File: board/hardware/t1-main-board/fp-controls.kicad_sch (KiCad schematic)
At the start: 6 parts

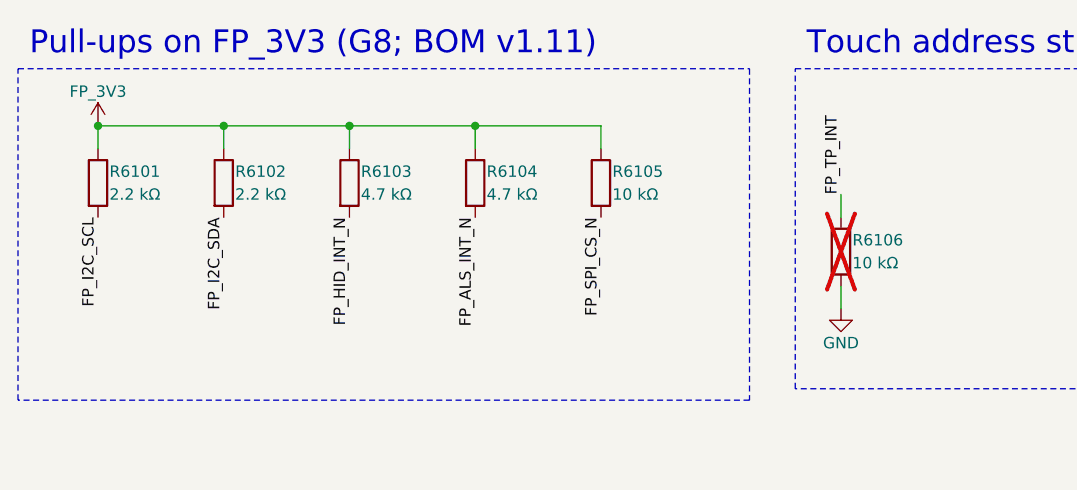
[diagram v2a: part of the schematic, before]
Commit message: NFC reader withdrawn from the board, every model (BRD-057)
Maintainer decision 2026-10-27, reason: board area. blk.nfc-reader (#42)
withdrawn: PN7160, front end, crystal, antenna contacts, NFC_VBAT switch
and link #18 removed (35 parts). BRD-057 reworded: NFC as the dynamic tag
only; blk.nfc-tag stays. Pinout v1: 1N20, A37, B38 become unconnected
spares, expander P05 a spare. BOM v1.18 item 7 (line 50: 5 switches,
lines 127-128 withdrawn), power tree v0.10, variant files, feature blocks.

Sheets after the removed one move up a page; references renumbered in
plan.py, parts.py and the specs (J6201 -> J6101 and others).

Placement v1.4: 990 parts placed, board need 96.9 % (99.1 % before),
factor 1.72; 243 capacitors within bound; DRC 0 errors; ERC 0 errors;
craft Q1 met; overlaps 0; pcb tests pass; STEP exported.

Co-Authored-By: Claude Opus 5.5 <noreply@anthropic.com>
Claude-Session: https://claude.ai/code/session_01Ei262h3TpgY9vyfNLMi5Mn
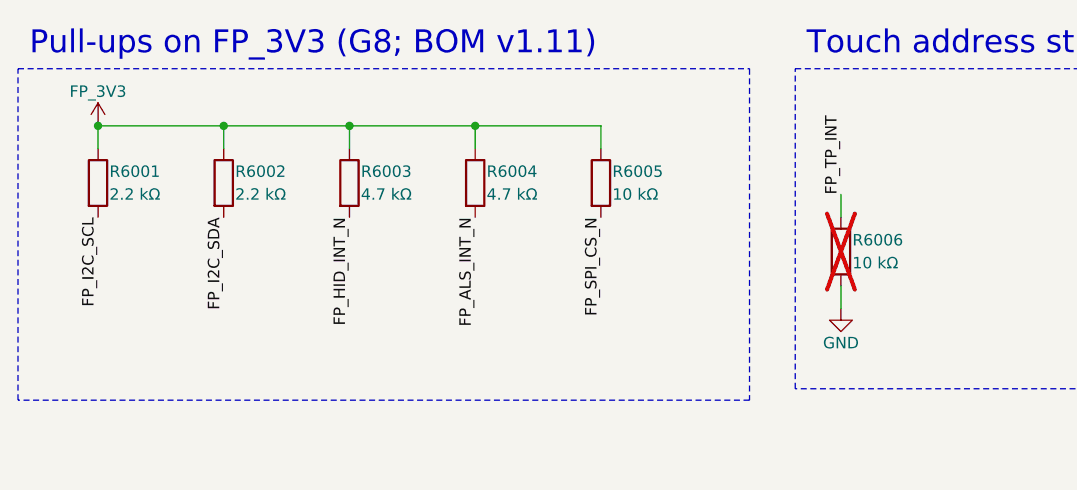
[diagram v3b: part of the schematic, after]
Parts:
- removed R6101, R6102: 2.2 kΩ, Resistor_SMD:R_0201_0603Metric, symbol Device:R
- removed R6103, R6104: 4.7 kΩ, Resistor_SMD:R_0201_0603Metric, symbol Device:R
- removed R6105, R6106: 10 kΩ, Resistor_SMD:R_0201_0603Metric, symbol Device:R
- added R6001, R6002: 2.2 kΩ, Resistor_SMD:R_0201_0603Metric, symbol Device:R
- added R6003, R6004: 4.7 kΩ, Resistor_SMD:R_0201_0603Metric, symbol Device:R
- added R6005, R6006: 10 kΩ, Resistor_SMD:R_0201_0603Metric, symbol Device:R
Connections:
- net FP_3V3: now also R6001.1, R6002.1, R6003.1, R6004.1, R6005.1
- net FP_ALS_INT_N: now also R6004.2
- net FP_HID_INT_N: now also R6003.2
- net FP_I2C_SCL: now also R6001.2
- net FP_I2C_SDA: now also R6002.2
- net FP_SPI_CS_N: now also R6005.2
- net FP_TP_INT: now also R6006.1
- net GND: now also R6006.2
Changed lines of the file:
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@@
 (title_block (title "Faceplate controls") (date "2026-10-25") (rev "A") (company "The OpenDAP Project") (comment 1 "blk.fp-controls") (comment 2 "I2C3, SPI/DBI and interrupt pulls on FP_3V3, the touch address strap"))
 (symbol (lib_id "Device:R") (at 31.75 48.26 0) (unit 1) (body_style 1) (exclude_from_sim no) (in_bom yes) (on_board yes) (dnp no)
-  (property "Reference" "R6101" (at 33.02 46.99 0) (effects (font (size 1.27 1.27)) (justify left)))
+  (property "Reference" "R6001" (at 33.02 46.99 0) (effects (font (size 1.27 1.27)) (justify left)))
   (property "Value" "2.2 kΩ" (at 33.02 49.53 0) (effects (font (size 1.27 1.27)) (justify left)))
   (property "Footprint" "Resistor_SMD:R_0201_0603Metric" (at 31.75 48.26 0) (effects (font (size 1.27 1.27))) (hide yes))
@@
   (pin "1")
   (pin "2")
-  (instances (project "t1-main-board" (path "/7746052e-d7f9-59ad-ba73-bd2b74439529/d44150e6-4ff4-595e-8942-92097db7bcde" (reference "R6101") (unit 1))))
+  (instances (project "t1-main-board" (path "/7746052e-d7f9-59ad-ba73-bd2b74439529/d44150e6-4ff4-595e-8942-92097db7bcde" (reference "R6001") (unit 1))))
 )
 (wire (pts (xy 31.75 44.45) (xy 31.75 41.91)) (stroke (width 0) (type default)))
 (symbol (lib_id "Device:R") (at 45.72 48.26 0) (unit 1) (body_style 1) (exclude_from_sim no) (in_bom yes) (on_board yes) (dnp no)
-  (property "Reference" "R6102" (at 46.99 46.99 0) (effects (font (size 1.27 1.27)) (justify left)))
+  (property "Reference" "R6002" (at 46.99 46.99 0) (effects (font (size 1.27 1.27)) (justify left)))
   (property "Value" "2.2 kΩ" (at 46.99 49.53 0) (effects (font (size 1.27 1.27)) (justify left)))
   (property "Footprint" "Resistor_SMD:R_0201_0603Metric" (at 45.72 48.26 0) (effects (font (size 1.27 1.27))) (hide yes))
@@
   (pin "1")
   (pin "2")
-  (instances (project "t1-main-board" (path "/7746052e-d7f9-59ad-ba73-bd2b74439529/d44150e6-4ff4-595e-8942-92097db7bcde" (reference "R6102") (unit 1))))
+  (instances (project "t1-main-board" (path "/7746052e-d7f9-59ad-ba73-bd2b74439529/d44150e6-4ff4-595e-8942-92097db7bcde" (reference "R6002") (unit 1))))
 )
 (wire (pts (xy 45.72 44.45) (xy 45.72 41.91)) (stroke (width 0) (type default)))
@@
 (junction (at 31.75 41.91) (diameter 0) (color 0 0 0 0))
 (symbol (lib_id "Device:R") (at 59.69 48.26 0) (unit 1) (body_style 1) (exclude_from_sim no) (in_bom yes) (on_board yes) (dnp no)
-  (property "Reference" "R6103" (at 60.96 46.99 0) (effects (font (size 1.27 1.27)) (justify left)))
+  (property "Reference" "R6003" (at 60.96 46.99 0) (effects (font (size 1.27 1.27)) (justify left)))
   (property "Value" "4.7 kΩ" (at 60.96 49.53 0) (effects (font (size 1.27 1.27)) (justify left)))
   (property "Footprint" "Resistor_SMD:R_0201_0603Metric" (at 59.69 48.26 0) (effects (font (size 1.27 1.27))) (hide yes))
@@
   (pin "1")
   (pin "2")
-  (instances (project "t1-main-board" (path "/7746052e-d7f9-59ad-ba73-bd2b74439529/d44150e6-4ff4-595e-8942-92097db7bcde" (reference "R6103") (unit 1))))
+  (instances (project "t1-main-board" (path "/7746052e-d7f9-59ad-ba73-bd2b74439529/d44150e6-4ff4-595e-8942-92097db7bcde" (reference "R6003") (unit 1))))
 )
 (wire (pts (xy 59.69 44.45) (xy 59.69 41.91)) (stroke (width 0) (type default)))
@@
 (junction (at 45.72 41.91) (diameter 0) (color 0 0 0 0))
 (symbol (lib_id "Device:R") (at 73.66 48.26 0) (unit 1) (body_style 1) (exclude_from_sim no) (in_bom yes) (on_board yes) (dnp no)
-  (property "Reference" "R6104" (at 74.93 46.99 0) (effects (font (size 1.27 1.27)) (justify left)))
+  (property "Reference" "R6004" (at 74.93 46.99 0) (effects (font (size 1.27 1.27)) (justify left)))
   (property "Value" "4.7 kΩ" (at 74.93 49.53 0) (effects (font (size 1.27 1.27)) (justify left)))
   (property "Footprint" "Resistor_SMD:R_0201_0603Metric" (at 73.66 48.26 0) (effects (font (size 1.27 1.27))) (hide yes))
@@
   (pin "1")
   (pin "2")
-  (instances (project "t1-main-board" (path "/7746052e-d7f9-59ad-ba73-bd2b74439529/d44150e6-4ff4-595e-8942-92097db7bcde" (reference "R6104") (unit 1))))
+  (instances (project "t1-main-board" (path "/7746052e-d7f9-59ad-ba73-bd2b74439529/d44150e6-4ff4-595e-8942-92097db7bcde" (reference "R6004") (unit 1))))
 )
 (wire (pts (xy 73.66 44.45) (xy 73.66 41.91)) (stroke (width 0) (type default)))
@@
 (junction (at 59.69 41.91) (diameter 0) (color 0 0 0 0))
 (symbol (lib_id "Device:R") (at 87.63 48.26 0) (unit 1) (body_style 1) (exclude_from_sim no) (in_bom yes) (on_board yes) (dnp no)
-  (property "Reference" "R6105" (at 88.9 46.99 0) (effects (font (size 1.27 1.27)) (justify left)))
+  (property "Reference" "R6005" (at 88.9 46.99 0) (effects (font (size 1.27 1.27)) (justify left)))
   (property "Value" "10 kΩ" (at 88.9 49.53 0) (effects (font (size 1.27 1.27)) (justify left)))
   (property "Footprint" "Resistor_SMD:R_0201_0603Metric" (at 87.63 48.26 0) (effects (font (size 1.27 1.27))) (hide yes))
@@
   (pin "1")
   (pin "2")
-  (instances (project "t1-main-board" (path "/7746052e-d7f9-59ad-ba73-bd2b74439529/d44150e6-4ff4-595e-8942-92097db7bcde" (reference "R6105") (unit 1))))
+  (instances (project "t1-main-board" (path "/7746052e-d7f9-59ad-ba73-bd2b74439529/d44150e6-4ff4-595e-8942-92097db7bcde" (reference "R6005") (unit 1))))
 )
 (wire (pts (xy 87.63 44.45) (xy 87.63 41.91)) (stroke (width 0) (type default)))
@@
 (text "Pull-ups on FP_3V3 (G8; BOM v1.11)" (exclude_from_sim no) (at 24.13 34.29 0) (effects (font (size 2.54 2.54)) (justify left bottom)))
 (symbol (lib_id "Device:R") (at 114.3 55.88 0) (unit 1) (body_style 1) (exclude_from_sim no) (in_bom yes) (on_board yes) (dnp yes)
-  (property "Reference" "R6106" (at 115.57 54.61 0) (effects (font (size 1.27 1.27)) (justify left)))
+  (property "Reference" "R6006" (at 115.57 54.61 0) (effects (font (size 1.27 1.27)) (justify left)))
   (property "Value" "10 kΩ" (at 115.57 57.15 0) (effects (font (size 1.27 1.27)) (justify left)))
   (property "Footprint" "Resistor_SMD:R_0201_0603Metric" (at 114.3 55.88 0) (effects (font (size 1.27 1.27))) (hide yes))
@@
   (pin "1")
   (pin "2")
-  (instances (project "t1-main-board" (path "/7746052e-d7f9-59ad-ba73-bd2b74439529/d44150e6-4ff4-595e-8942-92097db7bcde" (reference "R6106") (unit 1))))
+  (instances (project "t1-main-board" (path "/7746052e-d7f9-59ad-ba73-bd2b74439529/d44150e6-4ff4-595e-8942-92097db7bcde" (reference "R6006") (unit 1))))
 )
 (wire (pts (xy 114.3 52.07) (xy 114.3 49.53)) (stroke (width 0) (type default)))

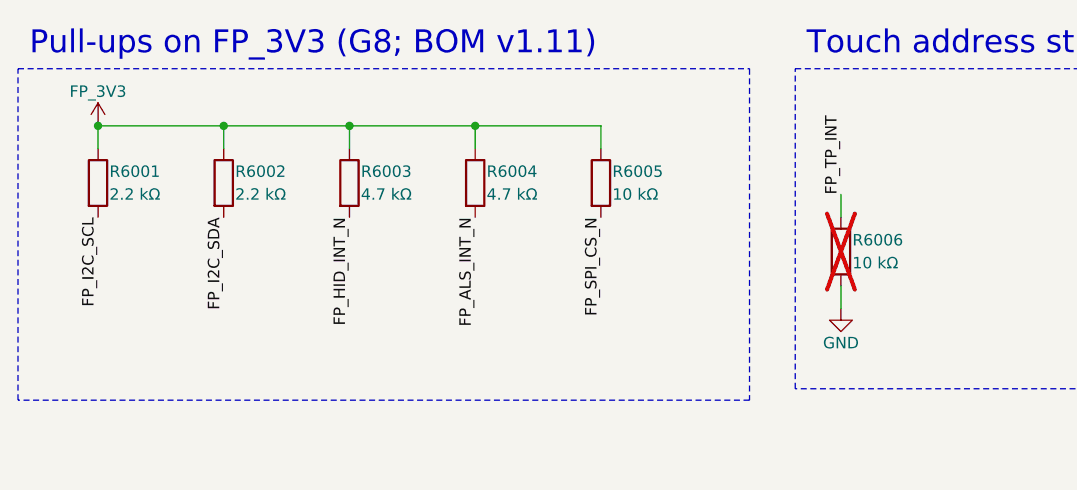
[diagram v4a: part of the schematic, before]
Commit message: Shield-can frames on the back (BOM v1.19, placement v1.6)
blk.shields: three etched two-piece frames made to order under the
amended T1-038, not fitted in either variant: SoC and LPDDR4X, the radio
module, the DACs and the back of the headphone stage. shields.toml holds
the geometry; pcb/shields.py derives land, keep-outs and courtyard ring;
the generator draws the lands and the placer reserves them, with parts up
to 1.3 mm inside (PCB-Z-01). The sheet takes page 59, so the sheets from
fp-display on carry the next page (J6201, SW6901-SW6904).

Placement v1.6: 994 parts placed, 99.5 % board need (97.0 % before the
frames), factor 1.64, 244 capacitors within their bound, DRC 0 errors,
ERC 0 errors, craft Q1 met, pcb tests pass (31), STEP exported.

Co-Authored-By: Claude Opus 5.5 <noreply@anthropic.com>
Claude-Session: https://claude.ai/code/session_013P6pW9LdyEMFishwCcZGUr
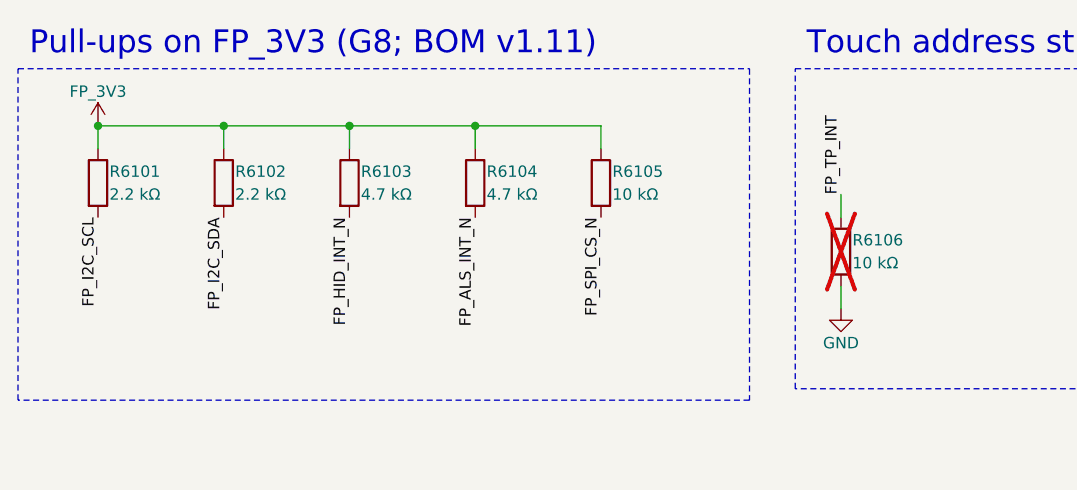
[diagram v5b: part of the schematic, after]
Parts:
- removed R6001, R6002: 2.2 kΩ, Resistor_SMD:R_0201_0603Metric, symbol Device:R
- removed R6003, R6004: 4.7 kΩ, Resistor_SMD:R_0201_0603Metric, symbol Device:R
- removed R6005, R6006: 10 kΩ, Resistor_SMD:R_0201_0603Metric, symbol Device:R
- added R6101, R6102: 2.2 kΩ, Resistor_SMD:R_0201_0603Metric, symbol Device:R
- added R6103, R6104: 4.7 kΩ, Resistor_SMD:R_0201_0603Metric, symbol Device:R
- added R6105, R6106: 10 kΩ, Resistor_SMD:R_0201_0603Metric, symbol Device:R
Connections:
- net FP_3V3: now also R6101.1, R6102.1, R6103.1, R6104.1, R6105.1
- net FP_ALS_INT_N: now also R6104.2
- net FP_HID_INT_N: now also R6103.2
- net FP_I2C_SCL: now also R6101.2
- net FP_I2C_SDA: now also R6102.2
- net FP_SPI_CS_N: now also R6105.2
- net FP_TP_INT: now also R6106.1
- net GND: now also R6106.2
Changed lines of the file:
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@@
 (title_block (title "Faceplate controls") (date "2026-10-25") (rev "A") (company "The OpenDAP Project") (comment 1 "blk.fp-controls") (comment 2 "I2C3, SPI/DBI and interrupt pulls on FP_3V3, the touch address strap"))
 (symbol (lib_id "Device:R") (at 31.75 48.26 0) (unit 1) (body_style 1) (exclude_from_sim no) (in_bom yes) (on_board yes) (dnp no)
-  (property "Reference" "R6001" (at 33.02 46.99 0) (effects (font (size 1.27 1.27)) (justify left)))
+  (property "Reference" "R6101" (at 33.02 46.99 0) (effects (font (size 1.27 1.27)) (justify left)))
   (property "Value" "2.2 kΩ" (at 33.02 49.53 0) (effects (font (size 1.27 1.27)) (justify left)))
   (property "Footprint" "Resistor_SMD:R_0201_0603Metric" (at 31.75 48.26 0) (effects (font (size 1.27 1.27))) (hide yes))
@@
   (pin "1")
   (pin "2")
-  (instances (project "t1-main-board" (path "/7746052e-d7f9-59ad-ba73-bd2b74439529/d44150e6-4ff4-595e-8942-92097db7bcde" (reference "R6001") (unit 1))))
+  (instances (project "t1-main-board" (path "/7746052e-d7f9-59ad-ba73-bd2b74439529/d44150e6-4ff4-595e-8942-92097db7bcde" (reference "R6101") (unit 1))))
 )
 (wire (pts (xy 31.75 44.45) (xy 31.75 41.91)) (stroke (width 0) (type default)))
 (symbol (lib_id "Device:R") (at 45.72 48.26 0) (unit 1) (body_style 1) (exclude_from_sim no) (in_bom yes) (on_board yes) (dnp no)
-  (property "Reference" "R6002" (at 46.99 46.99 0) (effects (font (size 1.27 1.27)) (justify left)))
+  (property "Reference" "R6102" (at 46.99 46.99 0) (effects (font (size 1.27 1.27)) (justify left)))
   (property "Value" "2.2 kΩ" (at 46.99 49.53 0) (effects (font (size 1.27 1.27)) (justify left)))
   (property "Footprint" "Resistor_SMD:R_0201_0603Metric" (at 45.72 48.26 0) (effects (font (size 1.27 1.27))) (hide yes))
@@
   (pin "1")
   (pin "2")
-  (instances (project "t1-main-board" (path "/7746052e-d7f9-59ad-ba73-bd2b74439529/d44150e6-4ff4-595e-8942-92097db7bcde" (reference "R6002") (unit 1))))
+  (instances (project "t1-main-board" (path "/7746052e-d7f9-59ad-ba73-bd2b74439529/d44150e6-4ff4-595e-8942-92097db7bcde" (reference "R6102") (unit 1))))
 )
 (wire (pts (xy 45.72 44.45) (xy 45.72 41.91)) (stroke (width 0) (type default)))
@@
 (junction (at 31.75 41.91) (diameter 0) (color 0 0 0 0))
 (symbol (lib_id "Device:R") (at 59.69 48.26 0) (unit 1) (body_style 1) (exclude_from_sim no) (in_bom yes) (on_board yes) (dnp no)
-  (property "Reference" "R6003" (at 60.96 46.99 0) (effects (font (size 1.27 1.27)) (justify left)))
+  (property "Reference" "R6103" (at 60.96 46.99 0) (effects (font (size 1.27 1.27)) (justify left)))
   (property "Value" "4.7 kΩ" (at 60.96 49.53 0) (effects (font (size 1.27 1.27)) (justify left)))
   (property "Footprint" "Resistor_SMD:R_0201_0603Metric" (at 59.69 48.26 0) (effects (font (size 1.27 1.27))) (hide yes))
@@
   (pin "1")
   (pin "2")
-  (instances (project "t1-main-board" (path "/7746052e-d7f9-59ad-ba73-bd2b74439529/d44150e6-4ff4-595e-8942-92097db7bcde" (reference "R6003") (unit 1))))
+  (instances (project "t1-main-board" (path "/7746052e-d7f9-59ad-ba73-bd2b74439529/d44150e6-4ff4-595e-8942-92097db7bcde" (reference "R6103") (unit 1))))
 )
 (wire (pts (xy 59.69 44.45) (xy 59.69 41.91)) (stroke (width 0) (type default)))
@@
 (junction (at 45.72 41.91) (diameter 0) (color 0 0 0 0))
 (symbol (lib_id "Device:R") (at 73.66 48.26 0) (unit 1) (body_style 1) (exclude_from_sim no) (in_bom yes) (on_board yes) (dnp no)
-  (property "Reference" "R6004" (at 74.93 46.99 0) (effects (font (size 1.27 1.27)) (justify left)))
+  (property "Reference" "R6104" (at 74.93 46.99 0) (effects (font (size 1.27 1.27)) (justify left)))
   (property "Value" "4.7 kΩ" (at 74.93 49.53 0) (effects (font (size 1.27 1.27)) (justify left)))
   (property "Footprint" "Resistor_SMD:R_0201_0603Metric" (at 73.66 48.26 0) (effects (font (size 1.27 1.27))) (hide yes))
@@
   (pin "1")
   (pin "2")
-  (instances (project "t1-main-board" (path "/7746052e-d7f9-59ad-ba73-bd2b74439529/d44150e6-4ff4-595e-8942-92097db7bcde" (reference "R6004") (unit 1))))
+  (instances (project "t1-main-board" (path "/7746052e-d7f9-59ad-ba73-bd2b74439529/d44150e6-4ff4-595e-8942-92097db7bcde" (reference "R6104") (unit 1))))
 )
 (wire (pts (xy 73.66 44.45) (xy 73.66 41.91)) (stroke (width 0) (type default)))
@@
 (junction (at 59.69 41.91) (diameter 0) (color 0 0 0 0))
 (symbol (lib_id "Device:R") (at 87.63 48.26 0) (unit 1) (body_style 1) (exclude_from_sim no) (in_bom yes) (on_board yes) (dnp no)
-  (property "Reference" "R6005" (at 88.9 46.99 0) (effects (font (size 1.27 1.27)) (justify left)))
+  (property "Reference" "R6105" (at 88.9 46.99 0) (effects (font (size 1.27 1.27)) (justify left)))
   (property "Value" "10 kΩ" (at 88.9 49.53 0) (effects (font (size 1.27 1.27)) (justify left)))
   (property "Footprint" "Resistor_SMD:R_0201_0603Metric" (at 87.63 48.26 0) (effects (font (size 1.27 1.27))) (hide yes))
@@
   (pin "1")
   (pin "2")
-  (instances (project "t1-main-board" (path "/7746052e-d7f9-59ad-ba73-bd2b74439529/d44150e6-4ff4-595e-8942-92097db7bcde" (reference "R6005") (unit 1))))
+  (instances (project "t1-main-board" (path "/7746052e-d7f9-59ad-ba73-bd2b74439529/d44150e6-4ff4-595e-8942-92097db7bcde" (reference "R6105") (unit 1))))
 )
 (wire (pts (xy 87.63 44.45) (xy 87.63 41.91)) (stroke (width 0) (type default)))
@@
 (text "Pull-ups on FP_3V3 (G8; BOM v1.11)" (exclude_from_sim no) (at 24.13 34.29 0) (effects (font (size 2.54 2.54)) (justify left bottom)))
 (symbol (lib_id "Device:R") (at 114.3 55.88 0) (unit 1) (body_style 1) (exclude_from_sim no) (in_bom yes) (on_board yes) (dnp yes)
-  (property "Reference" "R6006" (at 115.57 54.61 0) (effects (font (size 1.27 1.27)) (justify left)))
+  (property "Reference" "R6106" (at 115.57 54.61 0) (effects (font (size 1.27 1.27)) (justify left)))
   (property "Value" "10 kΩ" (at 115.57 57.15 0) (effects (font (size 1.27 1.27)) (justify left)))
   (property "Footprint" "Resistor_SMD:R_0201_0603Metric" (at 114.3 55.88 0) (effects (font (size 1.27 1.27))) (hide yes))
@@
   (pin "1")
   (pin "2")
-  (instances (project "t1-main-board" (path "/7746052e-d7f9-59ad-ba73-bd2b74439529/d44150e6-4ff4-595e-8942-92097db7bcde" (reference "R6006") (unit 1))))
+  (instances (project "t1-main-board" (path "/7746052e-d7f9-59ad-ba73-bd2b74439529/d44150e6-4ff4-595e-8942-92097db7bcde" (reference "R6106") (unit 1))))
 )
 (wire (pts (xy 114.3 52.07) (xy 114.3 49.53)) (stroke (width 0) (type default)))
